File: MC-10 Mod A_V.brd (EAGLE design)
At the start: 60 x 34.9 mm, 28 parts, among them K1 PG203J, Q1 BC327, Q2 BC338, U1 MC1372, X1 3.579545

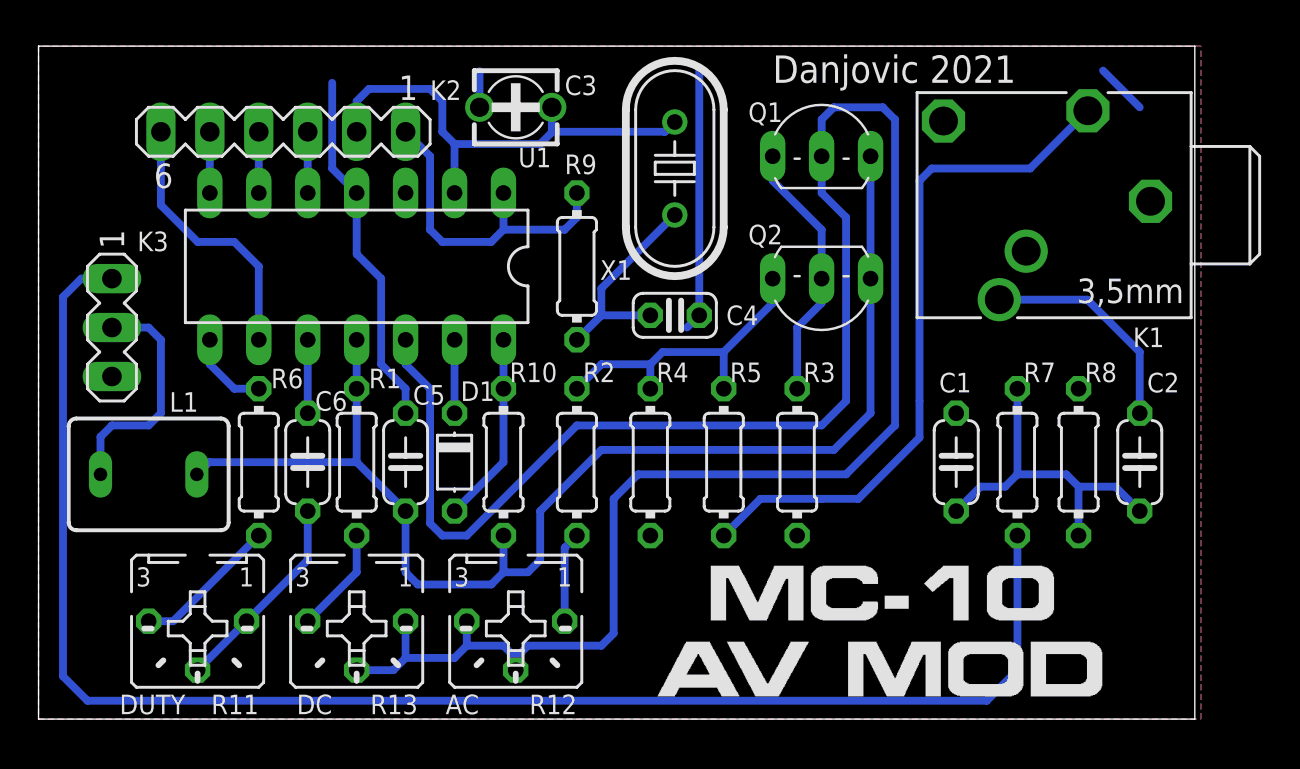
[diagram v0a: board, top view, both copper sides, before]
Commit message: Updated PCB for AV Mod
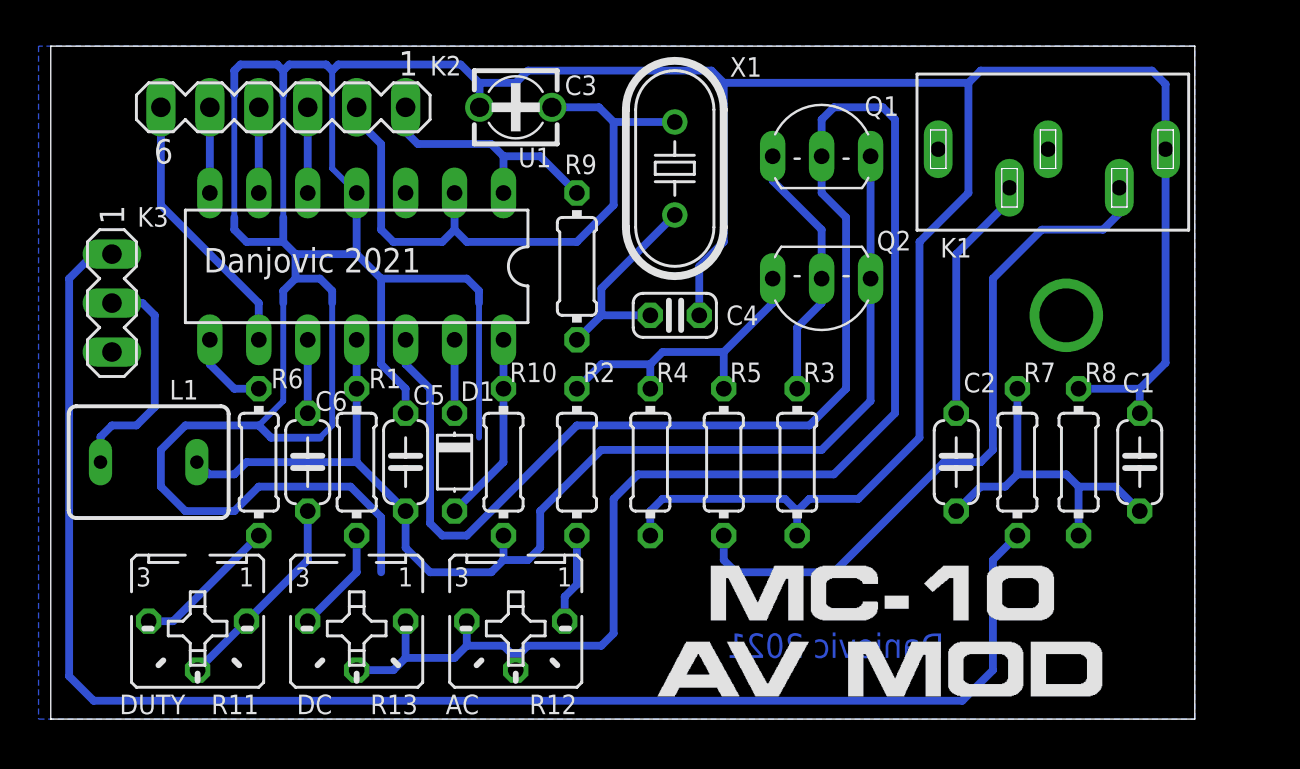
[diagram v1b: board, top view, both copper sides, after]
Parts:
- K1: value PG203J -> PJ-325; device con-hirschmann:PG203J -> AudioJack:PJ325
- moved C1 9.52 mm to (57.1, 13.3)
- moved C2 9.52 mm to (47.6, 13.3)
- moved K1 7.24 mm to (59.7, 28.6)
- moved K2 1.27 mm to (12.7, 31.8)
- moved K3 1.27 mm to (3.81, 21.6)
- moved L1 0.64 mm to (5.71, 13.3)
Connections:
- net N$5: now also K1.3; no longer K1.2
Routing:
- net GND: track 36.9 -> 226.2 mm, vias 0 -> 1
- net X1: track 24.8 -> 33.8 mm
- net CLK-OUT: track 17.2 -> 13.4 mm
- net VCC: track 66.5 -> 64.1 mm
- net CREF: track 3.18 -> 4.45 mm
- net CHB: track 3.18 -> 4.45 mm
- net CHA: track 3.18 -> 4.45 mm
- net N$5: track 11.6 -> 12.8 mm
- net N$7: track 111.8 -> 111.0 mm
- removed copper zone on layer 1, net GND
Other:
- board size 60 x 34.9 mm -> 59.4 x 34.9 mm

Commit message: Updated AV mod Schematics and PCB
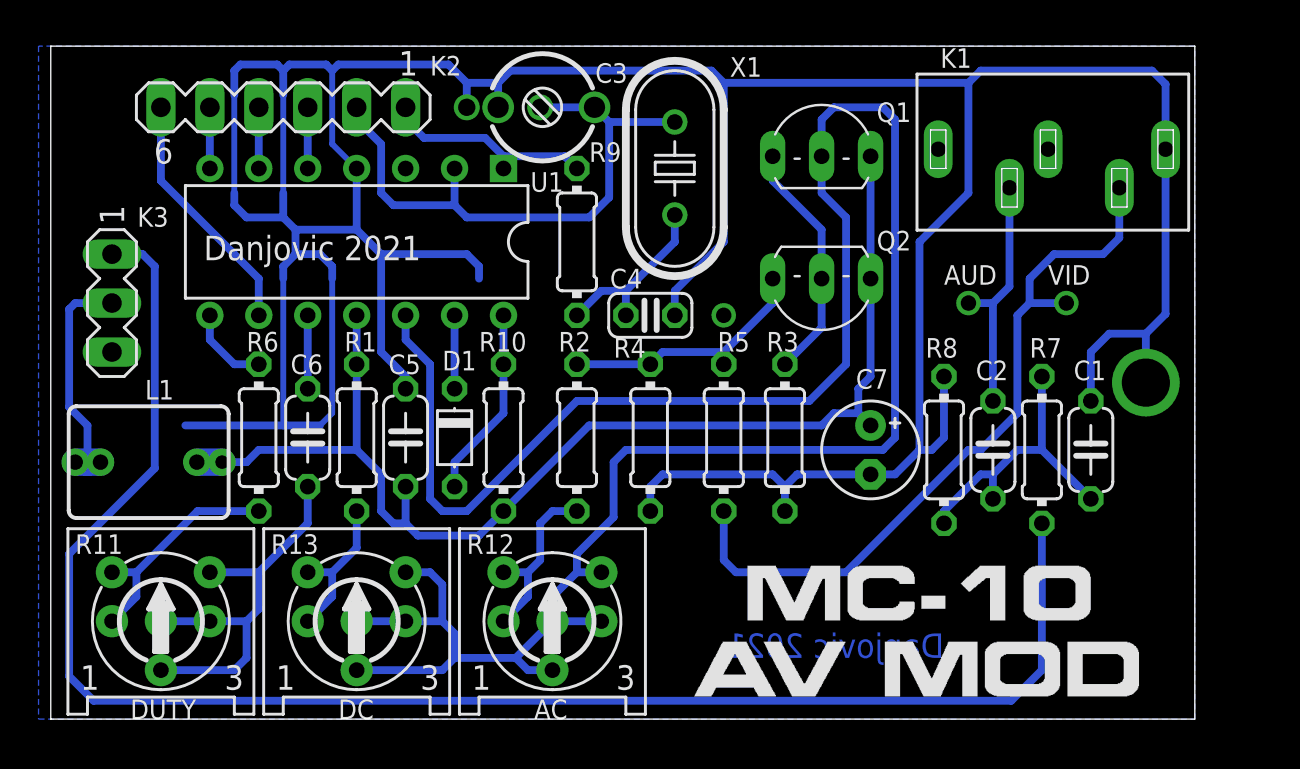
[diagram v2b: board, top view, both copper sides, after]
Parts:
- added C7: 47u, rcl:E2,5-5
- C3: value 20p -> 20PF; device c-trimm:3008 -> rcl:CTRIM3050.504
- D1: value 1N4148 -> 4148
- Q1: value BC327 -> BC560
- R11, R12, R13: device pot:B25P -> pot:RS3
- moved R8 7.01 mm to (47.0, 14.0)
- moved C1 2.62 mm to (54.6, 14.0)
- moved C2 2.01 mm to (49.5, 14.0)
- moved R11 1.91 mm to (6.35, 5.08), turned to 0 degrees
- moved R12 1.91 mm to (26.7, 5.08), turned to 0 degrees
- moved C3 1.59 mm to (26.4, 31.8)
- moved R7 1.42 mm to (52.1, 14.0)
- moved R3 1.42 mm to (38.7, 14.6)
- moved C4 1.27 mm to (31.8, 21.0)
- moved C5 1.27 mm to (19.1, 14.6)
- moved C6 1.27 mm to (14.0, 14.6)
- moved D1 1.27 mm to (21.6, 14.6)
- moved R1 1.27 mm to (16.5, 14.6)
- moved R10 1.27 mm to (24.1, 14.6)
- moved R2 1.27 mm to (27.9, 14.6)
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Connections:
- net N$2 renamed VID-OUT
- net N$5 renamed AUD-OUT
- removed net N$15: R11.E, R6.1
- new net N$6: R11.A, R6.1
- net GND: now also C3.2, C7.-; no longer C3.-
- net N$10: now also R13.A; no longer R13.E
- net N$11: now also R11.E; no longer R11.A
- net N$7: now also R13.E; no longer R13.A
- net VCC: now also C7.+
- net X1: now also C3.1; no longer C3.+
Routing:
- net GND: track 226.2 -> 204.1 mm, vias 1 -> 3
- net N$6: track 0.00 -> 12.0 mm, vias 0 -> 1
- net N$11: track 10.6 -> 21.9 mm, vias 0 -> 2
- net N$7: track 111.0 -> 121.7 mm, vias 0 -> 4
- net N$15: track 7.56 -> 0.00 mm
- net SOUND: track 80.0 -> 85.8 mm
- net N$14: track 4.71 -> 9.31 mm, vias 0 -> 1
- net N$13: track 16.4 -> 13.4 mm
- net X1: track 33.8 -> 31.2 mm, vias 0 -> 1
- net N$10: track 5.50 -> 8.04 mm, vias 0 -> 1
- net VID-OUT: track 36.3 -> 38.7 mm, vias 0 -> 1
- net N$3: track 18.1 -> 15.7 mm
- net CLK-OUT: track 13.4 -> 11.2 mm
- net N$9: track 11.1 -> 9.33 mm
- net LUMA: track 14.2 -> 12.9 mm
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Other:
- board text added: "AUD"
- board text added: "VID"
